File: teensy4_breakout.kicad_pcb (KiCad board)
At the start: 2 copper layers, 36.8 x 22.9 mm, 3 parts, among them J1 Edge A, J4 Edge B, U1 Teensy4.0

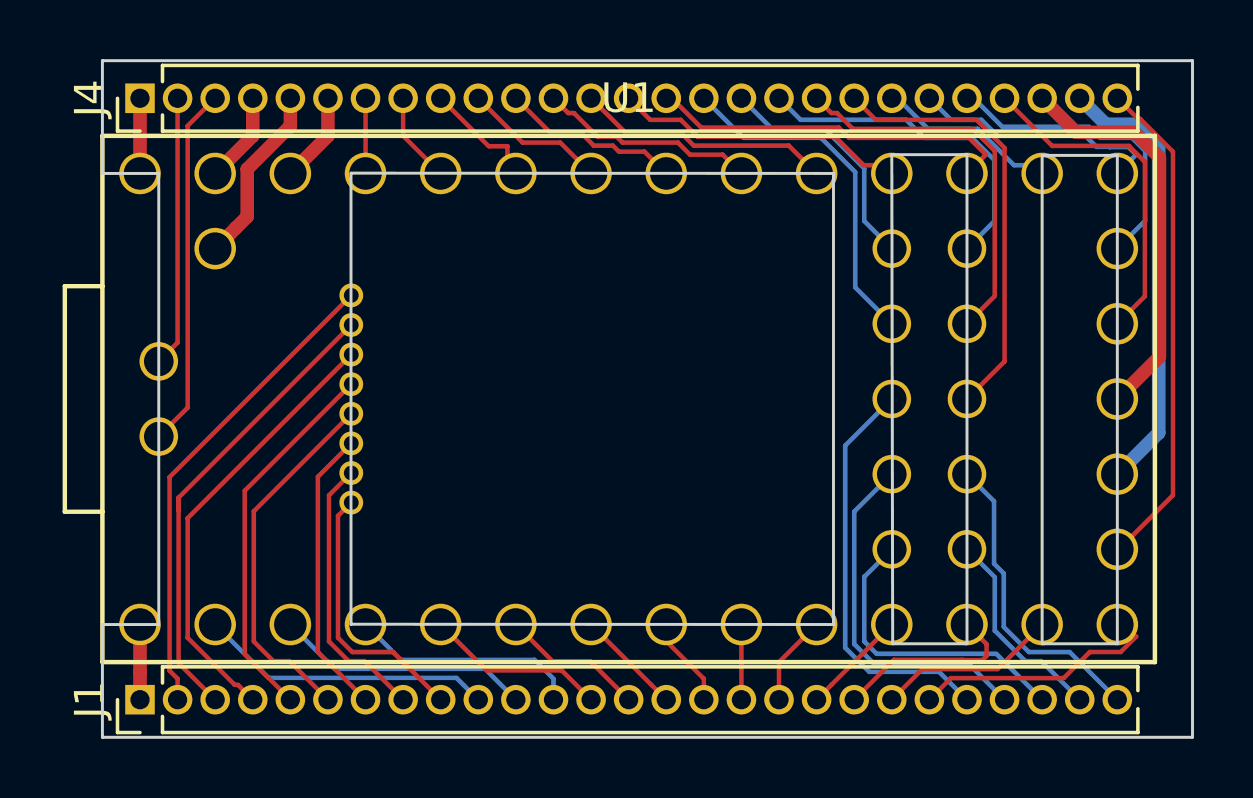
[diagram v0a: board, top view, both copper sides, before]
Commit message: Move outside edges to castellate the 0.05" header pins to facilitate direct soldering to board.  Pins can still be used, but a jig is required to solder them.
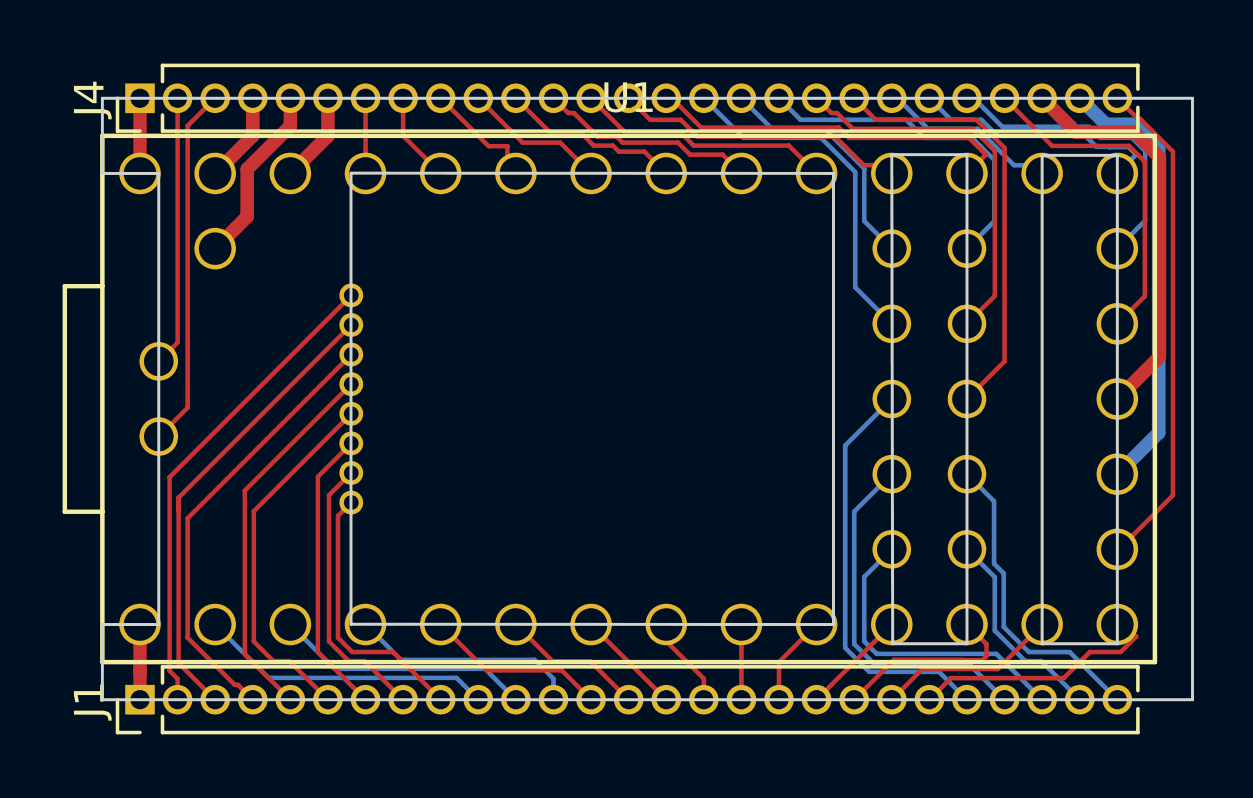
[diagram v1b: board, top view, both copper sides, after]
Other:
- board size 36.8 x 22.9 mm -> 36.8 x 20.3 mm
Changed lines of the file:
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@@
   (gr_line (start 107.95 66.7) (end 110.49 66.7) (layer Edge.Cuts) (width 0.1))
   (gr_line (start 102.87 66.675) (end 105.41 66.675) (layer Edge.Cuts) (width 0.1))
-  (gr_line (start 76.2 85.09) (end 76.2 86.36) (layer Edge.Cuts) (width 0.1))
-  (gr_line (start 76.2 63.5) (end 76.2 67.31) (layer Edge.Cuts) (width 0.1))
-  (gr_line (start 76.2 63.5) (end 113.03 63.5) (layer Edge.Cuts) (width 0.1))
+  (gr_line (start 76.2 85.09) (end 76.2 85.09) (layer Edge.Cuts) (width 0.1))
+  (gr_line (start 76.2 64.77) (end 76.2 67.31) (layer Edge.Cuts) (width 0.1))
+  (gr_line (start 76.2 64.77) (end 113.03 64.77) (layer Edge.Cuts) (width 0.1))
   (gr_line (start 100.9 67.31) (end 100.9 82.55) (layer Edge.Cuts) (width 0.1))
   (gr_line (start 84.6 67.3) (end 100.9 67.31) (layer Edge.Cuts) (width 0.1))
@@
   (gr_line (start 78.105 67.31) (end 78.105 82.55) (layer Edge.Cuts) (width 0.1))
   (gr_line (start 76.2 67.31) (end 78.105 67.31) (layer Edge.Cuts) (width 0.1))
-  (gr_line (start 113.03 86.36) (end 76.2 86.36) (layer Edge.Cuts) (width 0.1))
-  (gr_line (start 113.03 63.5) (end 113.03 86.36) (layer Edge.Cuts) (width 0.1))
+  (gr_line (start 113.03 85.09) (end 76.2 85.09) (layer Edge.Cuts) (width 0.1))
+  (gr_line (start 113.03 64.77) (end 113.03 85.09) (layer Edge.Cuts) (width 0.1))
   (segment (start 107.915412 83.785412) (end 107.377055 83.785412) (width 0.1524) (layer B.Cu) (net 1))
   (segment (start 109.22 85.09) (end 107.915412 83.785412) (width 0.1524) (layer B.Cu) (net 1))
